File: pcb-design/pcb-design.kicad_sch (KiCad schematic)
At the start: 19 parts, among them J1 Screw_Terminal_Motor, J2 Screw_Terminal_Heater, J3 Screw_Terminal_Heater, J4 Screw_Terminal_AC_Power, J5 Screw_Terminal_DC_Power, K1 ADW11, Q1 IRF3205, Q2 IRF3205, Q3 IRF3205, U1 DS18B20, U2 YAAJ_DCDC_StepDown_LM2596, U3 A4988_STEPPER_MOTOR_DRIVER_CA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, U4 ESP32-DEVKIT-V1

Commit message: design
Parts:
- removed U3: A4988_STEPPER_MOTOR_DRIVER_CARRIER, local_lib:A4988_motor, symbol local_lib:A4988_STEPPER_MOTOR_DRIVER_CARRIER
- added C1: C 16V 100nF, Capacitor_THT:C_Disc_D7.5mm_W5.0mm_P7.50mm, symbol Device:C
- added U3: TMC2209_SILENTSTEPSTICK, local_lib:MODULE_TMC2209_SILENTSTEPSTICK, symbol local_lib:TMC2209_SILENTSTEPSTICK
- J1: footprint TerminalBlock_4Ucon:TerminalBlock_4Ucon_1x02_P3.50mm_Vertical -> TerminalBlock:TerminalBlock_Altech_AK300-4_P5.00mm
- J2, J4, J5: footprint TerminalBlock_4Ucon:TerminalBlock_4Ucon_1x02_P3.50mm_Horizontal -> TerminalBlock:TerminalBlock_Altech_AK300-2_P5.00mm
- J3: value Screw_Terminal_Heater -> Screw_Terminal_Bubler; footprint TerminalBlock_4Ucon:TerminalBlock_4Ucon_1x02_P3.50mm_Horizontal -> TerminalBlock:TerminalBlock_Altech_AK300-2_P5.00mm
- R1, R2, R3, R4, R5, R6: footprint Resistor_THT:R_Axial_DIN0207_L6.3mm_D2.5mm_P2.54mm_Vertical -> Resistor_THT:R_Axial_DIN0207_L6.3mm_D2.5mm_P7.62mm_Horizontal
- U1: value DS18B20 -> DS18B20 - temperature sensor
- U4: footprint MODULE_ESP32_DEVKIT_V1 -> local_lib:MODULE_ESP32_DEVKIT_V1
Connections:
- net +12V: now also C1.2, U3.8 (VM)
- net +3.3V: now also U4.19 (D34), U3.2 (VIO)
- net GND: now also C1.1, U3.1 (GND), U3.16 (~{EN}), U3.7 (GND)
- net signal_dir: now also U4.20 (D35), U3.9 (DIR)
- net signal_step: now also U4.22 (D33), U3.10 (STEP)
- net at J1.2 (Pin_2): now also U3.5 (M2A)
- net at J1.1 (Pin_1): now also U3.4 (M1A)
- net at J1.3 (Pin_3): now also U3.3 (M1B)
- net at J1.4 (Pin_4): now also U3.6 (M2B)
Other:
- moved on the sheet: J1, J5, U2

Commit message: tests and corrections on final circuits
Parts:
- removed Q2: IRF3205, Package_TO_SOT_THT:TO-220-3_Vertical, symbol Transistor_FET:IRF3205
- added Q4, Q5: MT3203, Package_TO_SOT_THT:TO-220-3_Vertical, symbol Transistor_FET:IRF3205
- added R7: 4k7, symbol Device:R
- R1: value 10k -> 2k2
- R2: value 10k -> 100
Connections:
- net +12V: now also J2.2 (Pin_2)
- net +3.3V: now also U1.3 (V_{DD}), R7.1; no longer U1.2 (DQ), U4.19 (D34)
- net GND: now also Q4.3 (S), Q5.3 (S); no longer J2.2 (Pin_2), U1.3 (V_{DD})
- net ^signal_heater: no longer U4.4 (D2)
- net at R2.2: now also Q4.1 (G), Q5.1 (G)
- net at J2.1 (Pin_1): now also Q4.2 (D), Q5.2 (D)
- new net signal_temp_probe: R7.2, U1.2 (DQ), U4.19 (D34)
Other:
- moved on the sheet: J2, Q1, R1, R2, R3, U1

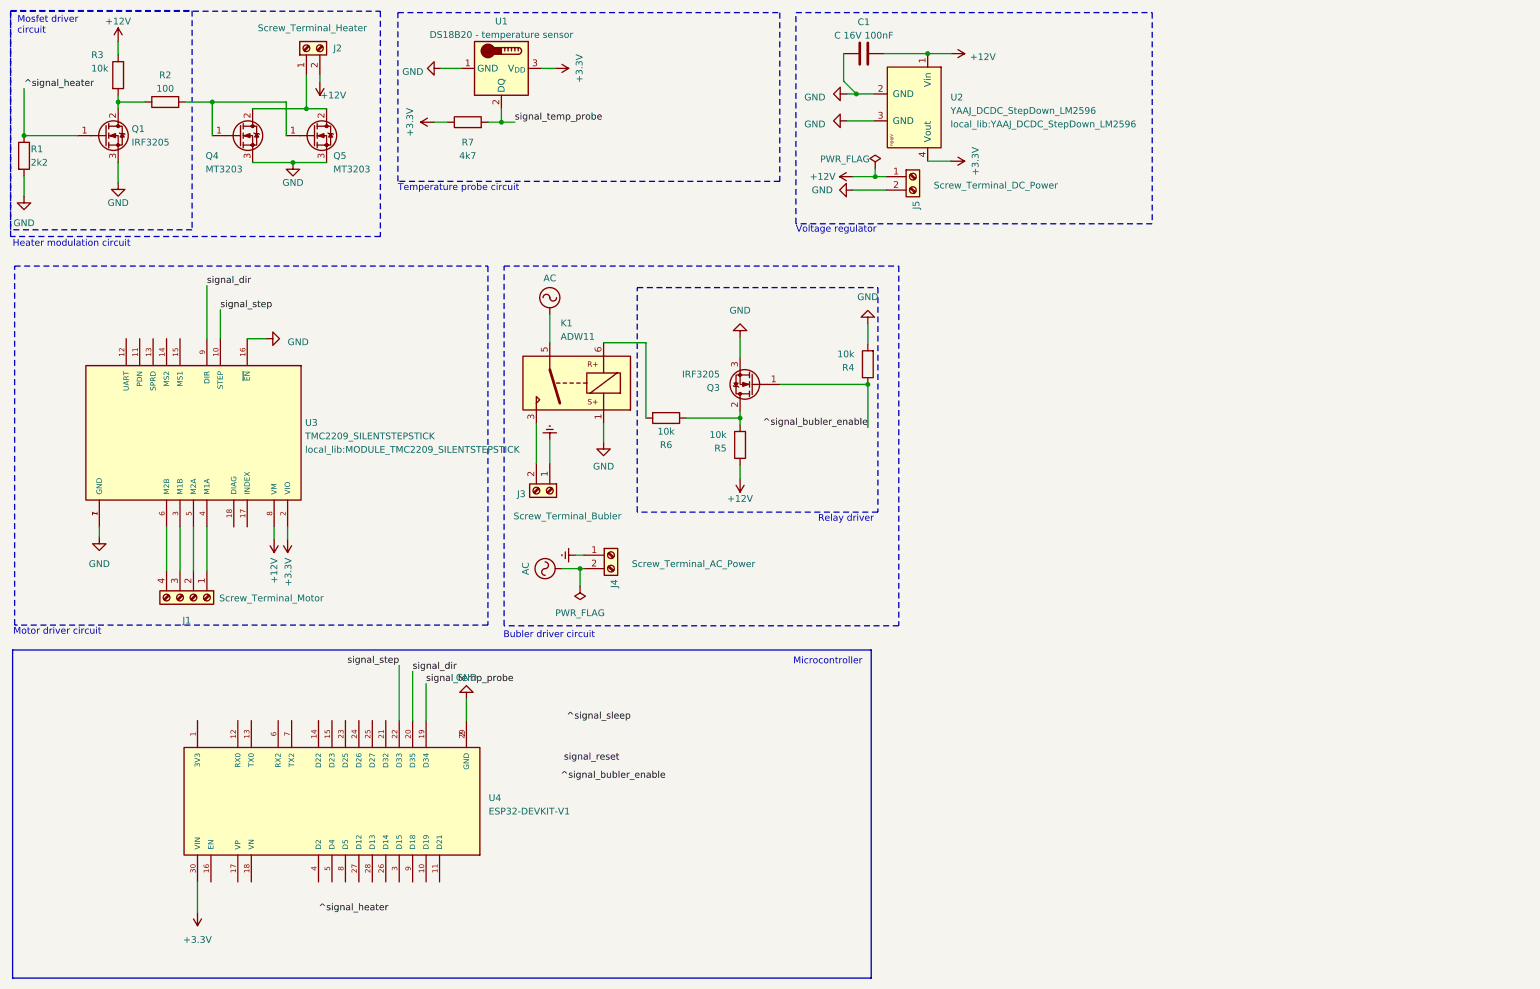
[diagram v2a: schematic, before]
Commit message: divided pcs
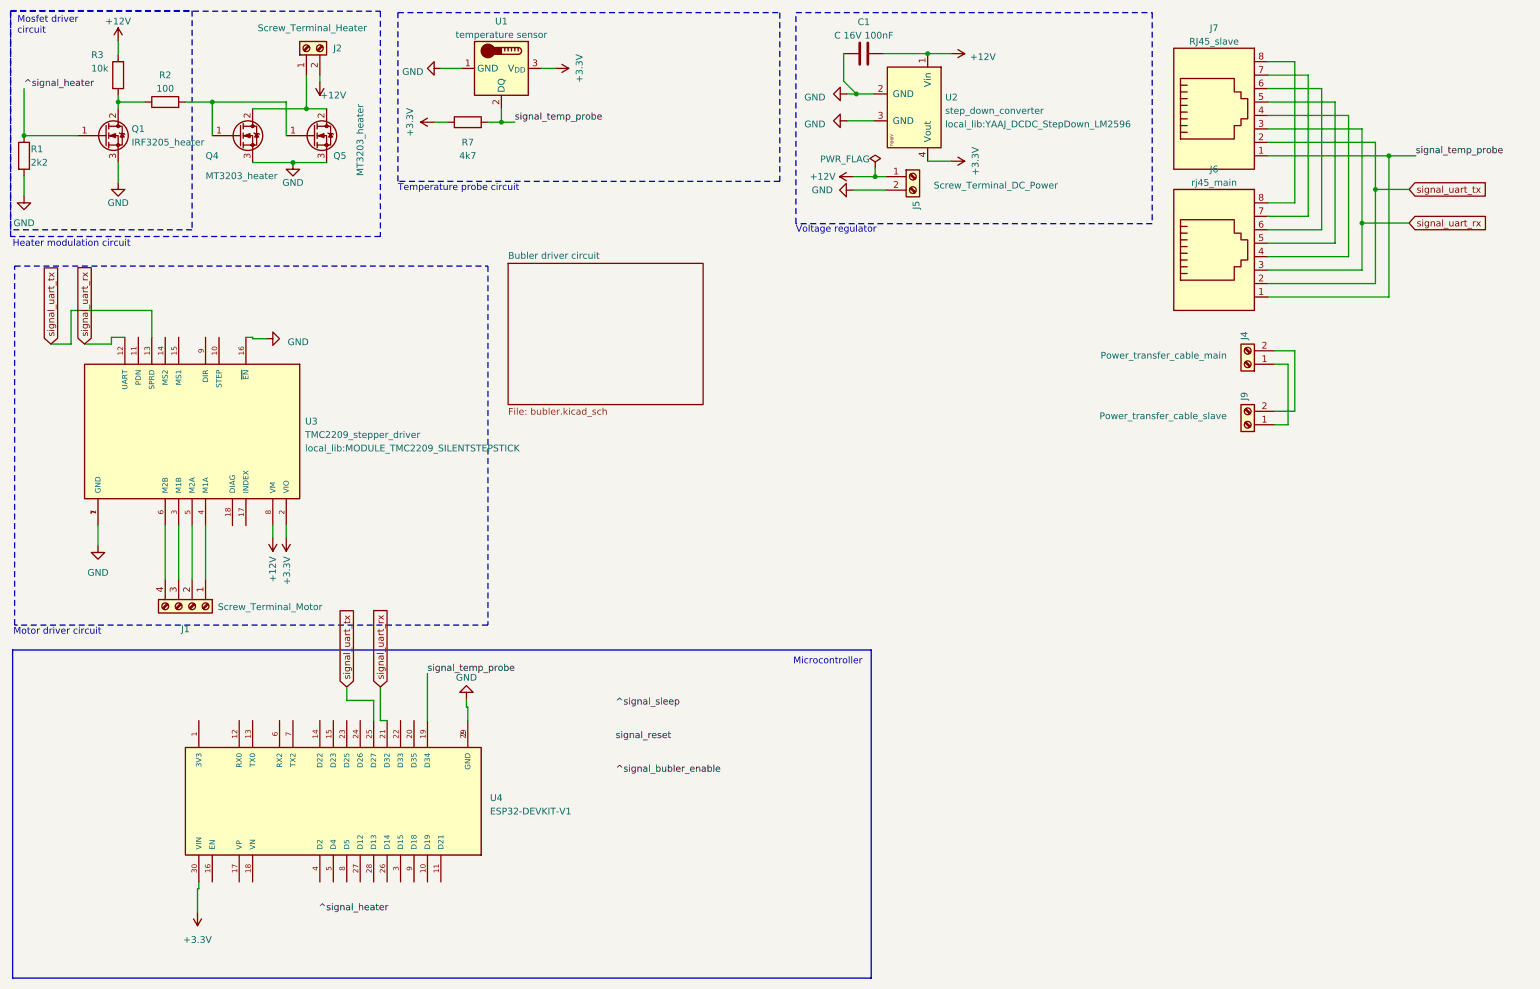
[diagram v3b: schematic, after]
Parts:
- removed J3: Screw_Terminal_Bubler, TerminalBlock:TerminalBlock_Altech_AK300-2_P5.00mm, symbol Connector:Screw_Terminal_01x02
- removed K1: ADW11, Relay_THT:Relay_1P1T_NO_10x24x18.8mm_Panasonic_ADW11xxxxW_THT, symbol Relay:ADW11
- removed Q3: IRF3205, Package_TO_SOT_THT:TO-220-3_Vertical, symbol Transistor_FET:IRF3205
- removed R4, R5, R6: 10k, Resistor_THT:R_Axial_DIN0207_L6.3mm_D2.5mm_P7.62mm_Horizontal, symbol Device:R
- added J6: rj45_main, Connector_RJ:RJ45_OST_PJ012-8P8CX_Vertical, symbol Connector:RJ45
- added J7: RJ45_slave, Connector_RJ:RJ45_OST_PJ012-8P8CX_Vertical, symbol Connector:RJ45
- added J9: Power_transfer_cable_slave, TerminalBlock:TerminalBlock_Altech_AK300-2_P5.00mm, symbol Connector:Screw_Terminal_01x02
- J4: value Screw_Terminal_AC_Power -> Power_transfer_cable_main
- Q1: value IRF3205 -> IRF3205_heater
- Q4, Q5: value MT3203 -> MT3203_heater
- R7: footprint (none) -> Resistor_THT:R_Axial_DIN0207_L6.3mm_D2.5mm_P7.62mm_Horizontal
- U1: value DS18B20 - temperature sensor -> temperature sensor
- U2: value YAAJ_DCDC_StepDown_LM2596 -> step_down_converter
- U3: value TMC2209_SILENTSTEPSTICK -> TMC2209_stepper_driver
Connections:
- net signal_temp_probe: now also J6.1, J7.1
- net signal_uart_rx: now reaches U4.21 (D32)
- net signal_uart_rx: now also U3.12 (UART), J6.3, J7.3
- net signal_uart_tx: now reaches U4.25 (D27)
- net signal_uart_tx: now also U3.13 (SPRD), J6.2, J7.2
- net AC: no longer names the net of J4.2 (Pin_2)
- net AC: now also J9.2 (Pin_2)
- net Earth: no longer names the net of J4.1 (Pin_1)
- net Earth: now also J9.1 (Pin_1)
- net signal_dir: no longer names the net of U4.20 (D35)
- net signal_dir: no longer U3.9 (DIR)
- net signal_step: no longer names the net of U4.22 (D33)
- net signal_step: no longer U3.10 (STEP)
- new net: J6.4, J7.4
- new net: J6.5, J7.5
- new net: J6.6, J7.6
- new net: J6.7, J7.7
- new net: J6.8, J7.8
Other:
- added sheet Bubler driver circuit (bubler.kicad_sch)
- note removed: "Bubler driver circuit"
- note removed: "Relay driver"
- moved on the sheet: J1
